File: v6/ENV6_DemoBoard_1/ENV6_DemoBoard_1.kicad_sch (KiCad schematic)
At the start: 0 parts

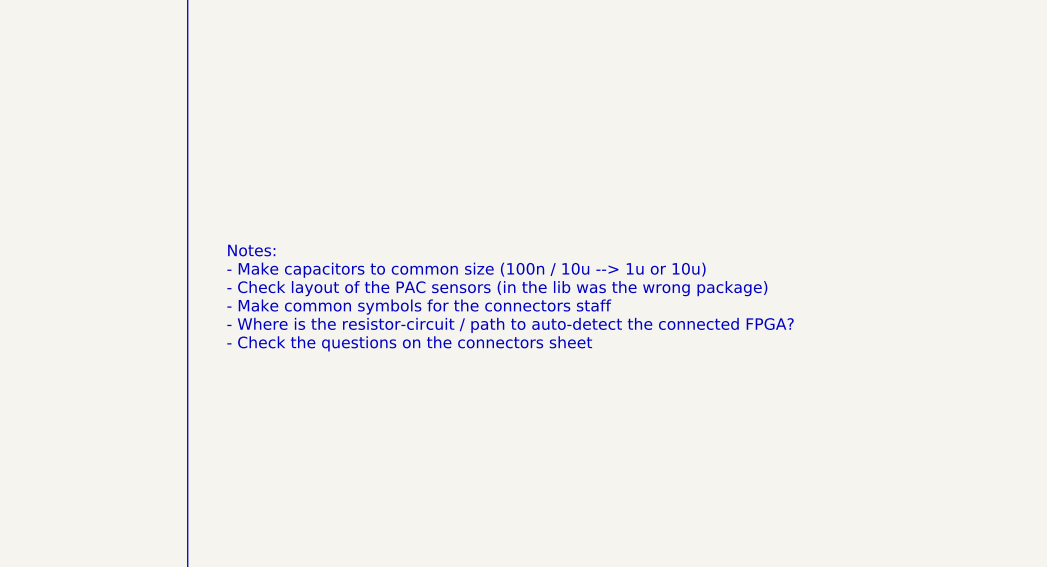
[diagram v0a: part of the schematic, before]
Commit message: SPartan7Board and new Symbol and Footprint
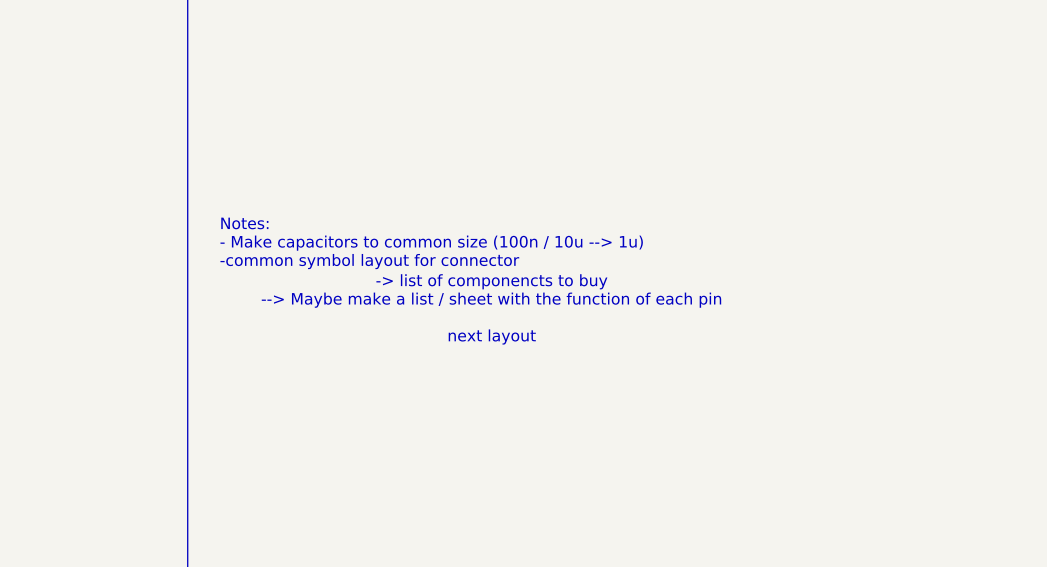
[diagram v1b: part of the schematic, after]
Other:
- note added: "-> list of componencts to buy --> Maybe make a list / sheet with the function of each pin next layout"
- note added: "Notes: - Make capacitors to common size (100n / 10u --> 1u) -common symbol layout for connector"
- note removed: "Notes: - Make capacitors to common size (100n / 10u --> 1u or 10u) - Check layout of the PAC sensors (in the lib was the wrong package) - Make common symbols for the connectors staff - Where is the resistor-circuit / path to auto-detect the connected FPGA? - Check the questions on the connectors sheet"
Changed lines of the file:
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@@
 		)
 	)
-	(text "Notes:\n- Make capacitors to common size (100n / 10u --> 1u or 10u)\n- Check layout of the PAC sensors (in the lib was the wrong package)\n- Make common symbols for the connectors staff\n- Where is the resistor-circuit / path to auto-detect the connected FPGA?\n- Check the questions on the connectors sheet"
+	(text "Notes:\n- Make capacitors to common size (100n / 10u --> 1u)\n-common symbol layout for connector"
 		(exclude_from_sim no)
-		(at 179.578 163.83 0)
+		(at 178.816 154.686 0)
 		(effects
 			(font
@@
 		(effects
 			(font
+				(size 1.27 1.27)
+			)
+		)
+	)
+	(text "-> list of componencts to buy\n--> Maybe make a list / sheet with the function of each pin\n\nnext layout"
+		(exclude_from_sim no)
+		(at 209.042 159.258 0)
+		(effects
+			(font

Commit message: Fix small errors for the design
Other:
- note added: "Notes: - ..."
- note removed: "-> list of componencts to buy --> Maybe make a list / sheet with the function of each pin next layout"
- note removed: "Notes: - Make capacitors to common size (100n / 10u --> 1u) -common symbol layout for connector"
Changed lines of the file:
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@@
 		)
 	)
-	(text "Notes:\n- Make capacitors to common size (100n / 10u --> 1u)\n-common symbol layout for connector"
+	(text "Notes:\n- ..."
 		(exclude_from_sim no)
-		(at 178.816 154.686 0)
+		(at 177.8 167.386 0)
 		(effects
 			(font
 				(size 1.27 1.27)
 			)
-			(justify left bottom)
+			(justify left top)
 		)
 	)
@@
 		(effects
 			(font
-				(size 1.27 1.27)
-			)
-		)
-	)
-	(text "-> list of componencts to buy\n--> Maybe make a list / sheet with the function of each pin\n\nnext layout"
-		(exclude_from_sim no)
-		(at 209.042 159.258 0)
-		(effects
-			(font
